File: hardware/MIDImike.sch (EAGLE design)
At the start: 5 parts, among them SW1 SPST, SW2 PUSH-BTN

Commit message: spring clean
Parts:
- removed SW2: PUSH-BTN, Coert-Vonk:PUSH-BTN
- added JP1: (no value), Coert-Vonk:JP2E
- SW1: value SPST -> PUSH-BTN; device Coert-Vonk:SPST -> Coert-Vonk:PUSH-BTN
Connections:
- net N$1 renamed A0
- removed net N$10: PCB1.IO.GAIN
- removed net N$8: PCB2.IO.D5, SW2.1
- new net REPLAY: PCB2.IO.D5, SW1.1
- net 5V: now also PCB1.IO.GAIN
- net GND: now also JP1.2; no longer SW2.2
- net N$3: now also JP1.3; no longer SW1.1
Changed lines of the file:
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@@
 <part name="GND2" library="Coert-Vonk" deviceset="GND" device=""/>
 <part name="GND3" library="Coert-Vonk" deviceset="GND" device=""/>
-<part name="SW2" library="Coert-Vonk" deviceset="PUSH-BTN" device=""/>
-<part name="SW1" library="Coert-Vonk" deviceset="SPST" device=""/>
+<part name="SW1" library="Coert-Vonk" deviceset="PUSH-BTN" device=""/>
 <part name="GND5" library="Coert-Vonk" deviceset="GND" device=""/>
 <part name="GND6" library="Coert-Vonk" deviceset="GND" device=""/>
@@
 <part name="PCB2" library="Coert-Vonk" deviceset="ARDUINO-UNO-R3" device=""/>
 <part name="P+4" library="Coert-Vonk" deviceset="5V" device=""/>
+<part name="JP1" library="Coert-Vonk" deviceset="JP2E" device="" package3d_urn="urn:adsk.eagle:package:15452/1"/>
 </parts>
 <sheets>
 <sheet>
 <plain>
-<text x="43.18" y="83.82" size="1.778" layer="91">USB-MIDI</text>
+<text x="40.64" y="88.9" size="1.778" layer="91" align="bottom-center">USB-MIDI</text>
 <text x="98.806" y="117.856" size="1.778" layer="91" align="bottom-center">REPLAY</text>
 <text x="55.88" y="66.04" size="1.778" layer="91" align="bottom-right">USB-MIDI or USB-SERIAL</text>
@@
 <attribute name="VALUE" x="99.06" y="134.62" size="1.778" layer="96" align="bottom-center"/>
 </instance>
-<instance part="SW2" gate="G$1" x="99.06" y="114.3" smashed="yes">
+<instance part="SW1" gate="G$1" x="99.06" y="114.3" smashed="yes">
 <attribute name="NAME" x="96.518090625" y="111.76381875" size="1.27" layer="95"/>
 <attribute name="VALUE" x="96.518190625" y="110.232390625" size="1.27" layer="96"/>
-</instance>
-<instance part="SW1" gate="G$1" x="48.26" y="81.28" smashed="yes">
-<attribute name="NAME" x="45.72" y="78.994" size="1.27" layer="95"/>
-<attribute name="VALUE" x="45.72" y="78.74" size="1.27" layer="96" align="top-left"/>
 </instance>
 <instance part="GND5" gate="1" x="40.64" y="76.2" smashed="yes">
@@
 <instance part="P+4" gate="1" x="45.72" y="121.92" smashed="yes">
 <attribute name="VALUE" x="45.72" y="123.19" size="1.778" layer="96" align="bottom-center"/>
+</instance>
+<instance part="JP1" gate="1" x="40.64" y="83.82" smashed="yes">
+<attribute name="NAME" x="45.72" y="85.09" size="1.778" layer="95" rot="R180" align="center-right"/>
+<attribute name="VALUE" x="46.355" y="83.82" size="1.778" layer="96" rot="R90"/>
 </instance>
 </instances>
@@
 </segment>
 <segment>
-<pinref part="GND5" gate="1" pin="GND"/>
-<wire x1="40.64" y1="78.74" x2="40.64" y2="81.28" width="0.1524" layer="91"/>
 <pinref part="SW1" gate="G$1" pin="2"/>
-<wire x1="40.64" y1="81.28" x2="43.18" y2="81.28" width="0.1524" layer="91"/>
-</segment>
-<segment>
-<pinref part="SW2" gate="G$1" pin="2"/>
 <wire x1="104.14" y1="114.3" x2="106.68" y2="114.3" width="0.1524" layer="91"/>
 <wire x1="106.68" y1="114.3" x2="106.68" y2="111.76" width="0.1524" layer="91"/>
 <pinref part="GND6" gate="1" pin="GND"/>
+</segment>
+<segment>
+<pinref part="GND5" gate="1" pin="GND"/>
+<pinref part="JP1" gate="1" pin="2"/>
+<wire x1="40.64" y1="81.28" x2="40.64" y2="78.74" width="0.1524" layer="91"/>
 </segment>
 </net>
@@
 <wire x1="111.76" y1="160.02" x2="111.76" y2="157.48" width="0.1524" layer="91"/>
 </segment>
-</net>
-<net name="N$1" class="0">
+<segment>
+<pinref part="PCB1" gate=".IO" pin="GAIN"/>
+<pinref part="P+4" gate="1" pin="5V"/>
+<wire x1="43.18" y1="116.84" x2="45.72" y2="116.84" width="0.1524" layer="91"/>
+<wire x1="45.72" y1="116.84" x2="45.72" y2="119.38" width="0.1524" layer="91"/>
+</segment>
+</net>
+<net name="A0" class="0">
 <segment>
 <wire x1="43.18" y1="114.3" x2="55.88" y2="114.3" width="0.1524" layer="91"/>
@@
 </segment>
 </net>
-<net name="N$3" class="0">
-<segment>
-<pinref part="SW1" gate="G$1" pin="1"/>
-<wire x1="53.34" y1="81.28" x2="55.88" y2="81.28" width="0.1524" layer="91"/>
-<pinref part="PCB2" gate=".IO" pin="MOSI2"/>
-</segment>
-</net>
-<net name="N$8" class="0">
+<net name="REPLAY" class="0">
 <segment>
 <wire x1="83.82" y1="106.68" x2="88.9" y2="106.68" width="0.1524" layer="91"/>
 <wire x1="88.9" y1="106.68" x2="88.9" y2="114.3" width="0.1524" layer="91"/>
-<pinref part="SW2" gate="G$1" pin="1"/>
+<pinref part="SW1" gate="G$1" pin="1"/>
 <wire x1="88.9" y1="114.3" x2="93.98" y2="114.3" width="0.1524" layer="91"/>
 <pinref part="PCB2" gate=".IO" pin="D5"/>
 </segment>
 </net>
-<net name="N$10" class="0">
-<segment>
-<wire x1="43.18" y1="116.84" x2="45.72" y2="116.84" width="0.1524" layer="91"/>
-<pinref part="PCB1" gate=".IO" pin="GAIN"/>
-<pinref part="P+4" gate="1" pin="5V"/>
-<wire x1="45.72" y1="119.38" x2="45.72" y2="116.84" width="0.1524" layer="91"/>
+<net name="N$3" class="0">
+<segment>
+<pinref part="PCB2" gate=".IO" pin="MOSI2"/>
+<pinref part="JP1" gate="1" pin="3"/>
+<wire x1="55.88" y1="81.28" x2="43.18" y2="81.28" width="0.1524" layer="91"/>
 </segment>
 </net>
@@
 </drawing>
 <compatibility>
+<note version="8.3" severity="warning">
+Since Version 8.3, EAGLE supports URNs for individual library
+assets (packages, symbols, and devices). The URNs of those assets
+will not be understood (or retained) with this version.
+</note>
+<note version="8.3" severity="warning">
+Since Version 8.3, EAGLE supports the association of 3D packages
+with devices in libraries, schematics, and board files. Those 3D
+packages will not be understood (or retained) with this version.
+</note>
 <note version="9.0" severity="warning">
 Since Version 9.0, EAGLE supports the align property for labels.

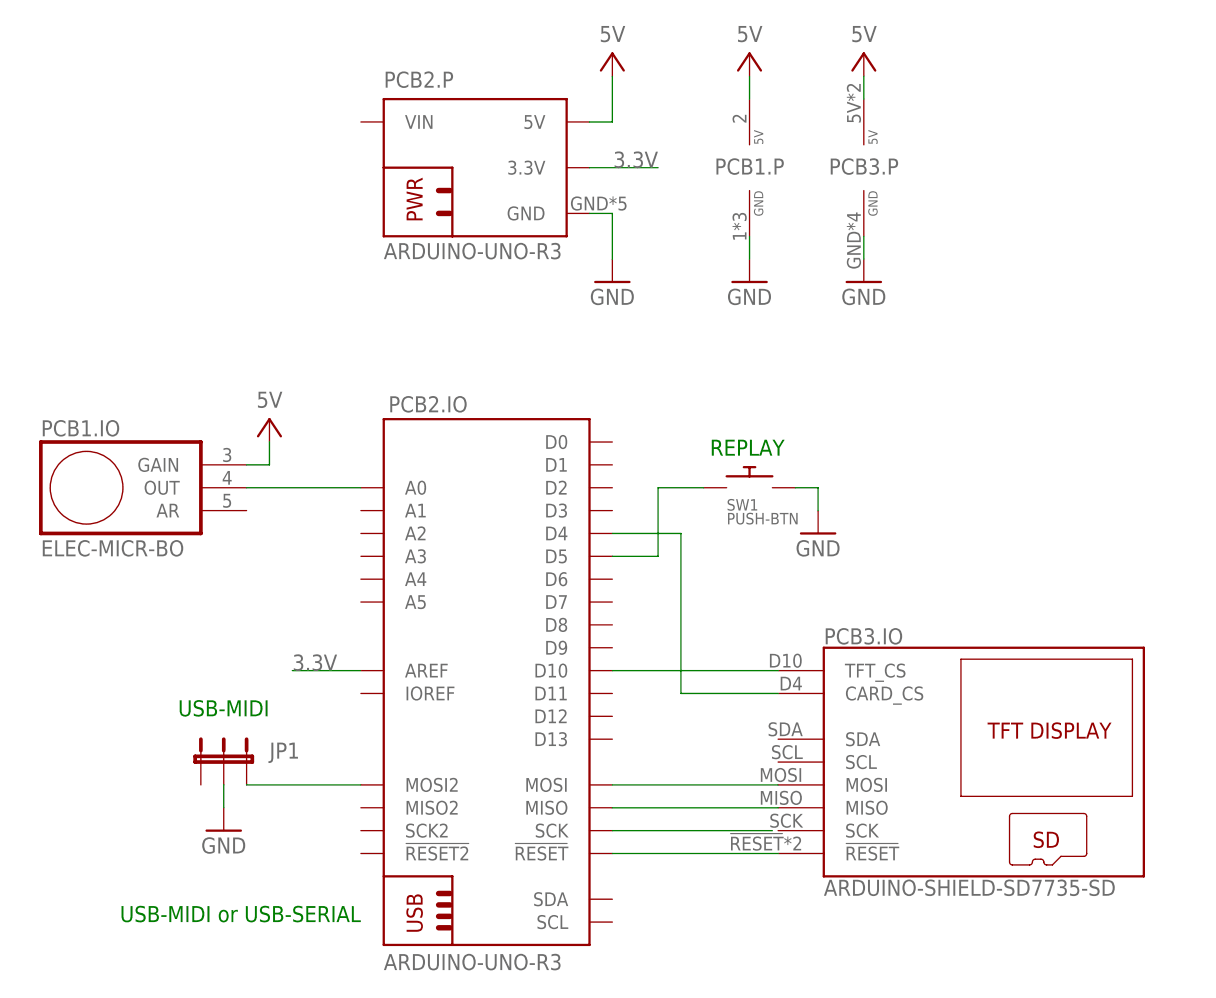
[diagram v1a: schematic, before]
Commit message: fix low notes; clean up
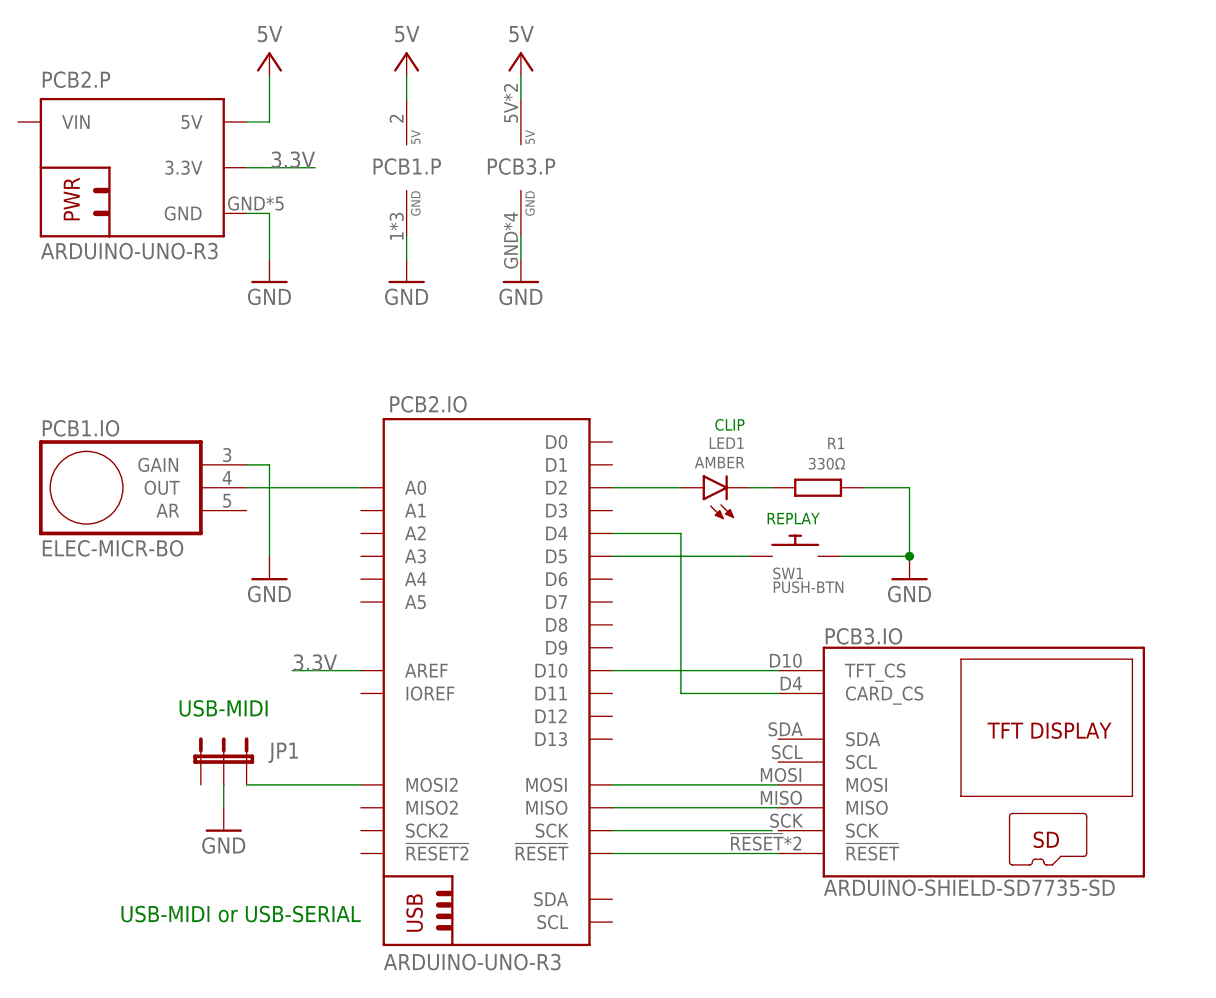
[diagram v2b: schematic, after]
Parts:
- added LED1: AMBER, OPNpool:LEDCHIPLED_0805
- added R1: 330Ω, rcl:R-EU_R0805
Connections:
- new net N$1: LED1.A, PCB2.IO.D2
- new net N$8: LED1.C, R1.2
- net 5V: no longer PCB1.IO.GAIN
- net GND: now also PCB1.IO.GAIN, R1.1
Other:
- note added: "CLIP"
- moved on the sheet: PCB1.P, PCB2.P, PCB3.P, SW1
